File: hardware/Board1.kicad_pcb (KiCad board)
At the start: 2 copper layers, 32.8 x 58.2 mm, 32 parts, among them IC1 AH1912-W-7, J1 DX07S016JA3R1500, J2 Conn_01x04_Pin, J2 USB_C_Receptacle_USB2.0, J3 Conn_ST_STDC14, J4 Conn_01x02_Pin, J5 Conn_01x02_Pin, SW1 SW_Push, U1 STM32F042G6U6TR, U2 TS2940CW33_RPG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

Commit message: final revision of the speed and cadence board
Finished re routing the PCB and also did BOM and production needed for JLC PCB
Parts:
- removed J1: DX07S016JA3R1500, DX07S016JA3R1500_USBC:CONN12_DX07S_JAE
- removed SW1: SW_Push, Button_Switch_SMD:SW_SPST_SKQG_WithStem
- added C10: 100n, Capacitor_SMD:C_0603_1608Metric, F.Cu at (130.0, 68.7)
- added C11: 100n, Capacitor_SMD:C_0603_1608Metric, F.Cu at (130.0, 71.2)
- added C12: 100nF, Capacitor_SMD:C_0603_1608Metric, F.Cu at (130.0, 73.7)
- added C4: 100n, Capacitor_SMD:C_0603_1608Metric, F.Cu at (126.0, 66.2)
- added C5: 100n, Capacitor_SMD:C_0603_1608Metric, F.Cu at (126.0, 68.7)
- added C6: 100n, Capacitor_SMD:C_0603_1608Metric, F.Cu at (126.0, 71.2)
- added C7: 100n, Capacitor_SMD:C_0603_1608Metric, F.Cu at (126.0, 73.7)
- added C8: 10n, Capacitor_SMD:C_0603_1608Metric, F.Cu at (126.0, 76.2)
- added C9: 1u, Capacitor_SMD:C_0603_1608Metric, F.Cu at (130.0, 66.2)
- added IC2: AH1912-W-7, Package_TO_SOT_SMD:SC-59, F.Cu at (121.5, 81.9)
- added R2: 10K, Resistor_SMD:R_0603_1608Metric, F.Cu at (130.0, 76.2)
- added SW2: SW_Push, Button_Switch_SMD:SW_SPST_SKQG_WithStem, F.Cu at (86.2, 57.0)
- added Y1: 8M, Crystal:Resonator_SMD_Murata_CSTxExxV-3Pin_3.0x1.1mm, F.Cu at (126.5, 79.2)
- U3: value STM32F072RBHx -> STM32F072RBTx; footprint Package_BGA:UFBGA-64_5x5mm_Layout8x8_P0.5mm -> Package_QFP:LQFP-64_10x10mm_P0.5mm
- moved U3 56.0 mm to (116.8, 72.2)
- moved C3 44.4 mm to (80.9, 87.2), turned to 180 degrees
- moved R4 44.1 mm to (80.9, 89.0)
- moved R5 43.8 mm to (80.9, 90.8), turned to 180 degrees
- moved U4 0.35 mm to (75.5, 89.5)
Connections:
- R6 pad 1: CAN_TX -> USB-
- R7 pad 1: CAN_RX -> USB+
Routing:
- net +5V: track 85.3 -> 0.00 mm, vias 1 -> 0
- net RESET_PROG: track 54.1 -> 0.00 mm
- net +3V3: track 49.9 -> 0.00 mm, vias 2 -> 0
- net Net-(IC1-OUTPUT): track 35.8 -> 0.00 mm, vias 1 -> 0
- net Prog_RX: track 34.2 -> 0.00 mm, vias 2 -> 0
- net Prog_TX: track 29.5 -> 0.00 mm, vias 2 -> 0
- net CAN_RX: track 27.5 -> 0.00 mm
- net CAN_TX: track 21.8 -> 0.00 mm, vias 2 -> 0
- net GND: track 18.8 -> 2.32 mm, vias 4 -> 0
- net codeclk: track 15.1 -> 0.00 mm
- net codeio: track 13.7 -> 0.00 mm
- net CAN+: track 11.0 -> 2.18 mm
- net CAN-: track 11.0 -> 2.38 mm
- net Net-(C3-Pad1): track 0.00 -> 3.52 mm
- net Net-(J1-CC2): track 2.69 -> 0.00 mm
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- removed copper zone on F.Cu, net GND

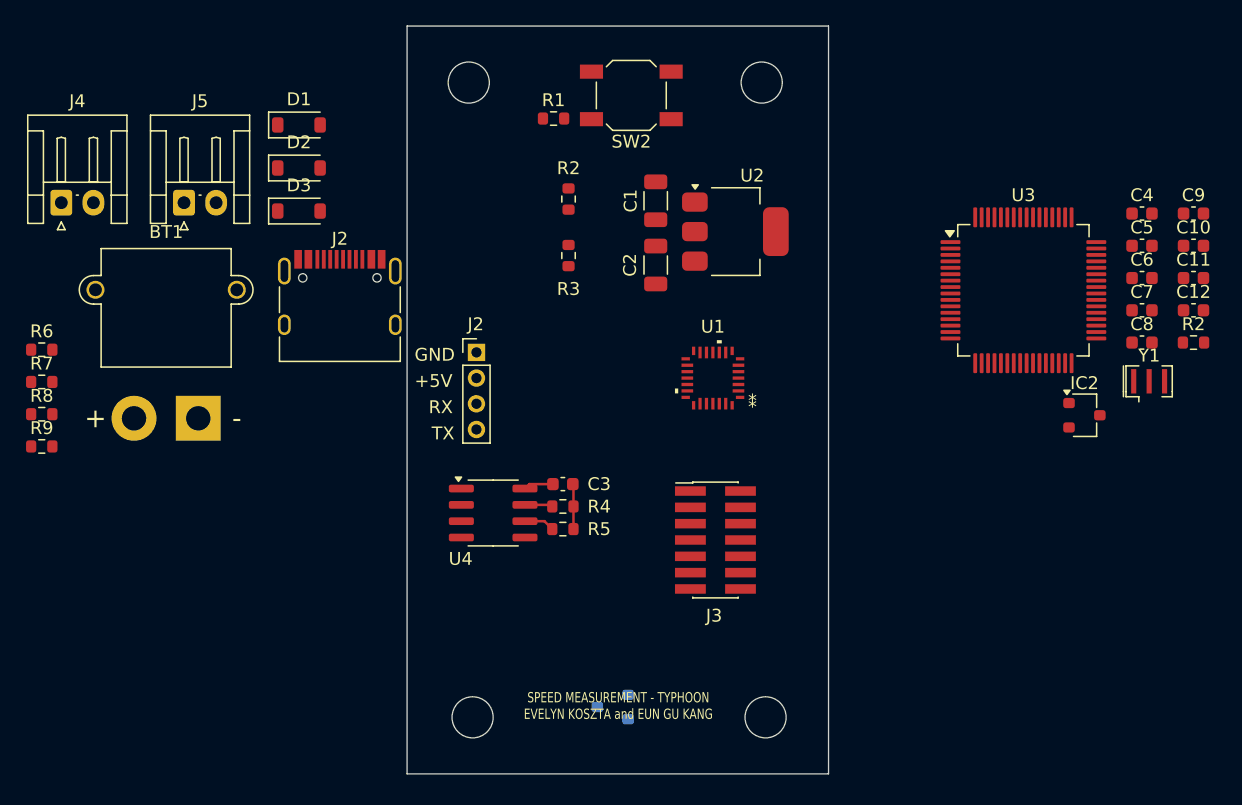
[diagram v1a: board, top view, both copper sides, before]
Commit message: Final small changes, only silkscreen stuff
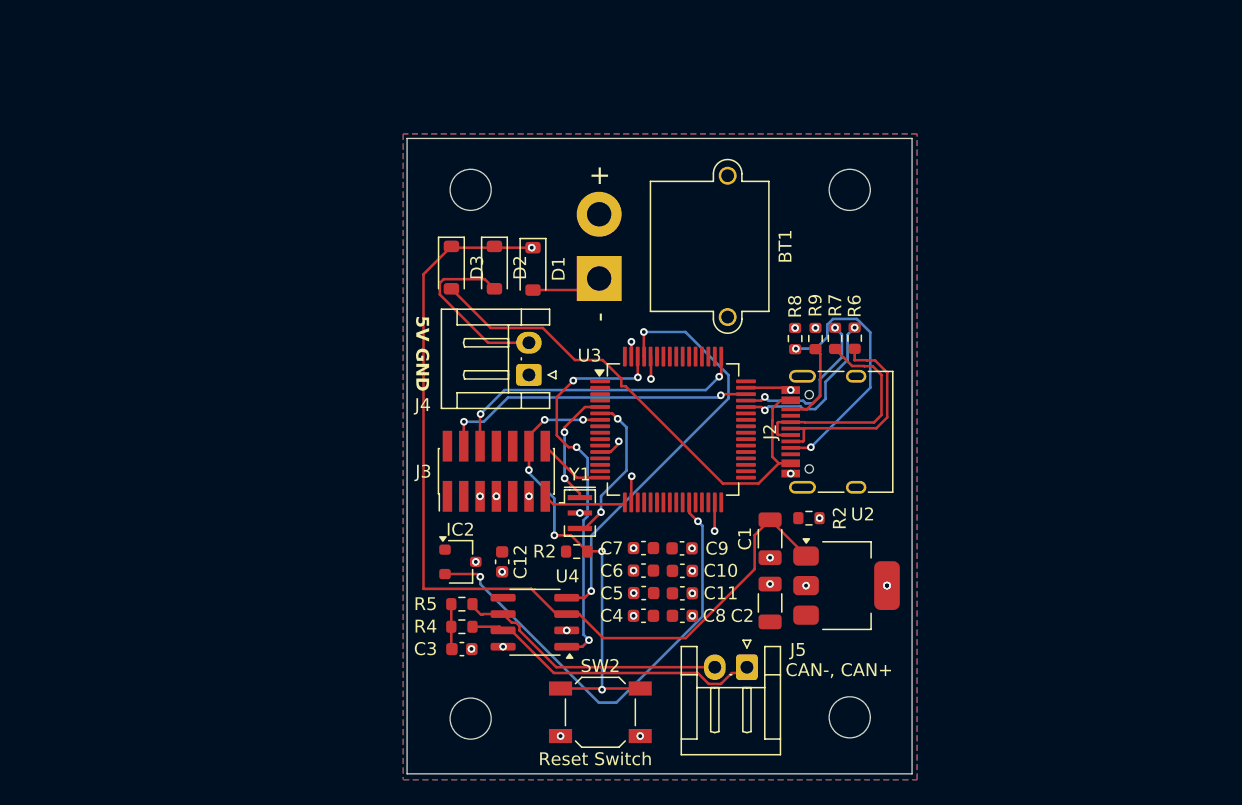
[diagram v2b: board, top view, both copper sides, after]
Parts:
- removed IC1: AH1912-W-7, Package_TO_SOT_SMD:SC-59
- removed the J2 at (74.2, 77.0)
- removed R1: 10K, Resistor_SMD:R_0603_1608Metric
- removed R3: 5.1k, Resistor_SMD:R_0603_1608Metric
- removed U1: STM32F042G6U6TR, STM32:UFQFPN28-4x4mm-M
- moved R6 63.3 mm to (103.6, 75.9), turned to -90 degrees
- moved R7 61.8 mm to (102.1, 75.9), turned to -90 degrees
- moved R9 60.8 mm to (100.6, 75.9), turned to -90 degrees
- moved R8 58.9 mm to (99.0, 75.9), turned to -90 degrees
- moved C12 57.3 mm to (76.2, 93.3), turned to -90 degrees
- moved J5 56.8 mm to (95.2, 101.5), turned to 180 degrees
- moved R2 50.7 mm to (82.0, 92.5)
- moved IC2 49.9 mm to (73.0, 93.3)
- moved C4 49.9 mm to (87.2, 97.5)
- moved SW2 48.1 mm to (83.8, 105.0), turned to 0 degrees
- moved C9 47.6 mm to (90.2, 92.2), turned to 180 degrees
- moved C5 47.3 mm to (87.2, 95.7)
- moved C10 47.1 mm to (90.2, 94.0), turned to 180 degrees
- moved C11 46.7 mm to (90.2, 95.8), turned to 180 degrees
- moved Y1 45.5 mm to (82.2, 89.5), turned to -90 degrees
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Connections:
- C10 pad 2: +3.3V -> +3V3
- C11 pad 2: +3.3V -> +3V3
- C12 pad 1: +3.3V -> +3V3
- C4 pad 2: +3.3V -> +3V3
- C5 pad 2: +3.3V -> +3V3
- C6 pad 2: +3.3V -> +3V3
- C7 pad 2: +3.3V -> +3V3
- C8 pad 2: +3.3V -> +3V3
- C9 pad 2: +3.3V -> +3V3
- IC2 pad 1: +3.3V -> +3V3
- R2 pad 1: +3.3V -> +3V3
- U3 pad 1: +3.3V -> +3V3
- U3 pad 13: +3.3V -> +3V3
- U3 pad 19: +3.3V -> +3V3
- U3 pad 32: +3.3V -> +3V3
- U3 pad 48: +3.3V -> +3V3
- U3 pad 64: +3.3V -> +3V3
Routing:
- net 5VA: track 0.00 -> 71.9 mm, vias 0 -> 1
- net +5VD: track 0.00 -> 39.8 mm
- net Net-(IC2-OUTPUT): track 0.00 -> 36.6 mm, vias 0 -> 2
- net RESET_PROG: track 0.00 -> 35.9 mm, vias 0 -> 6
- net CAN_RX: track 0.00 -> 33.3 mm, vias 0 -> 2
- net CAN_TX: track 0.00 -> 31.1 mm, vias 0 -> 4
- net codeio: track 0.00 -> 24.7 mm, vias 0 -> 2
- net codeclk: track 0.00 -> 23.9 mm, vias 0 -> 2
- net CAN+: track 2.18 -> 23.7 mm
- net Net-(J2-CC1): track 0.00 -> 20.2 mm, vias 0 -> 2
- net CAN-: track 2.38 -> 21.2 mm
- net /D-: track 0.00 -> 18.2 mm
- net /D+: track 0.00 -> 17.9 mm
- net +5V: track 0.00 -> 14.1 mm
- net USB-: track 0.00 -> 13.3 mm, vias 0 -> 2
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- added copper zone on F.Cu, net +3V3
- added copper zone on B.Cu, net GND
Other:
- board size 32.8 x 58.2 mm -> 39.3 x 49.4 mm
- board text added: "5V GND"
- board text added: "CAN-, CAN+"
- board text added: "Reset Switch"
- board text added: "SPEED MEASUREMENT - TYPHOON EVELYN KOSZTA and EUN GU KANG Revision: JUSTIN LO"
- board text removed: "+5V"
- board text removed: "GND"
- board text removed: "RX"
- board text removed: "SPEED MEASUREMENT - TYPHOON EVELYN KOSZTA and EUN GU KANG"
- board text removed: "TX"
